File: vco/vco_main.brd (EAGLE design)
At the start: 94.9 x 107.9 mm, 101 parts, among them IC1 OPA4130U, IC2 LM13700M, IC3 OPA4130U, IC4 OPA4130U, Q1 MMBFJ3

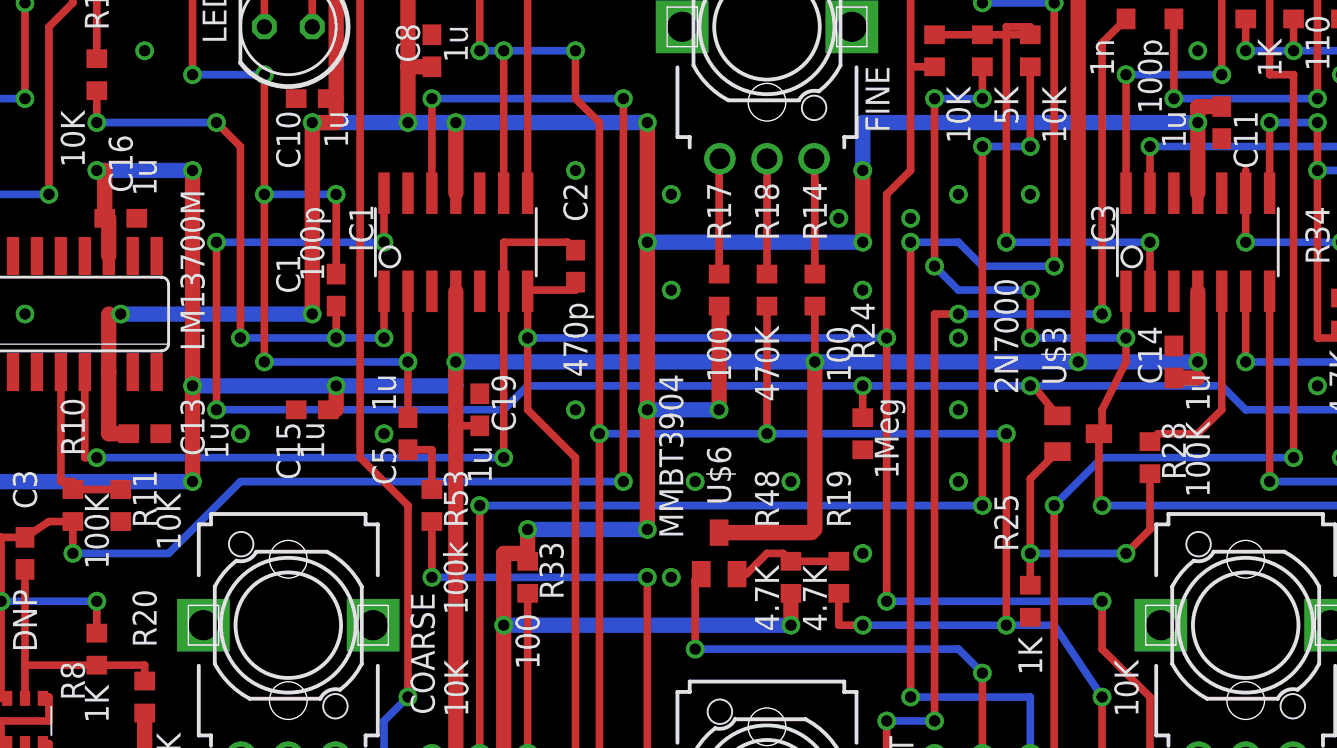
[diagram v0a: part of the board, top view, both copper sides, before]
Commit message: made some small changes that drove me crazy during assembly.
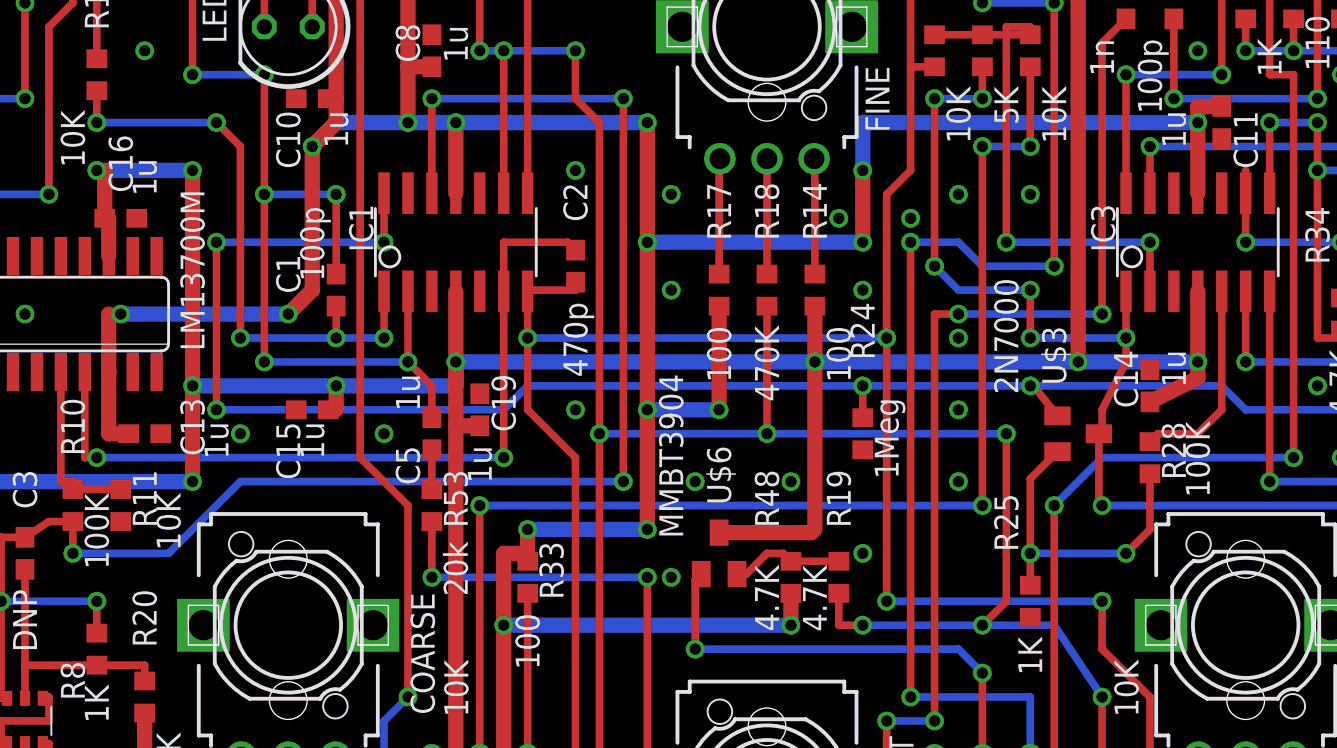
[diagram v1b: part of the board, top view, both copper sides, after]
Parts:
- R53: value 100k -> 20k
- moved C14 1.80 mm to (68.6, 67.3)
- moved C5 1.27 mm to (30.5, 64.8)
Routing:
- net +12V: track 255.3 -> 256.9 mm
- net N$48: track 3.38 -> 2.11 mm
- net -12V: track 342.7 -> 341.7 mm
- net N$5: track 195.6 -> 196.2 mm
- net N$3: track 67.6 -> 68.1 mm
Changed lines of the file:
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@@
 <setting verticaltext="up"/>
 </settings>
-<grid distance="0.5" unitdist="mil" unit="mil" style="lines" multiple="1" display="yes" altdistance="0.025" altunitdist="inch" altunit="inch"/>
+<grid distance="0.05" unitdist="inch" unit="inch" style="lines" multiple="1" display="no" altdistance="0.025" altunitdist="inch" altunit="inch"/>
 <layers>
 <layer number="1" name="Top" color="4" fill="1" visible="yes" active="yes"/>
@@
 </element>
 <element name="EXPMOD" library="dan" package="PJ301BM" value="PJ301BM" x="13.97" y="24.13" smashed="yes"/>
-<element name="C5" library="dan" package="C0603" value="1u" x="29.21" y="64.77" smashed="yes" rot="R270">
-<attribute name="NAME" x="27.305" y="64.135" size="1.27" layer="21" font="vector" ratio="15" rot="R270"/>
-<attribute name="VALUE" x="27.305" y="67.945" size="1.27" layer="21" font="vector" ratio="15" rot="R270"/>
+<element name="C5" library="dan" package="C0603" value="1u" x="30.48" y="64.77" smashed="yes" rot="R270">
+<attribute name="NAME" x="28.575" y="64.135" size="1.27" layer="21" font="vector" ratio="15" rot="R270"/>
+<attribute name="VALUE" x="28.575" y="67.945" size="1.27" layer="21" font="vector" ratio="15" rot="R270"/>
 </element>
 <element name="LINMOD" library="dan" package="PJ301BM" value="PJ301BM" x="31.75" y="8.89" smashed="yes"/>
@@
 <attribute name="VALUE" x="18.415" y="65.405" size="1.27" layer="21" font="vector" ratio="15" rot="R270"/>
 </element>
-<element name="C14" library="dan" package="C0603" value="1u" x="69.85" y="68.58" smashed="yes" rot="R90">
-<attribute name="NAME" x="67.945" y="70.485" size="1.27" layer="21" font="vector" ratio="15" rot="R270"/>
-<attribute name="VALUE" x="70.485" y="67.945" size="1.27" layer="21" font="vector" ratio="15" rot="R270"/>
+<element name="C14" library="dan" package="C0603" value="1u" x="68.58" y="67.31" smashed="yes" rot="R90">
+<attribute name="NAME" x="66.675" y="69.215" size="1.27" layer="21" font="vector" ratio="15" rot="R270"/>
+<attribute name="VALUE" x="69.215" y="69.215" size="1.27" layer="21" font="vector" ratio="15" rot="R270"/>
 </element>
 <element name="C15" library="dan" package="C0603" value="1u" x="24.13" y="66.04" smashed="yes" rot="R180">
@@
 <attribute name="VALUE" x="3.175" y="19.685" size="1.27" layer="21" font="vector" ratio="15" rot="R270"/>
 </element>
-<element name="R53" library="dan" package="R0603" value="100k" x="30.48" y="60.96" smashed="yes" rot="R90">
+<element name="R53" library="dan" package="R0603" value="20k" x="30.48" y="60.96" smashed="yes" rot="R90">
 <attribute name="NAME" x="31.115" y="62.865" size="1.27" layer="21" font="vector" ratio="15" rot="R270"/>
 <attribute name="VALUE" x="31.115" y="59.055" size="1.27" layer="21" font="vector" ratio="15" rot="R270"/>
@@
 <via x="25.4" y="77.47" extent="1-16" drill="0.6"/>
 <wire x1="25.4" y1="77.47" x2="25.4" y2="73.24" width="0.4064" layer="1"/>
-<wire x1="29.21" y1="68.58" x2="29.21" y2="65.62" width="0.4064" layer="1"/>
 <wire x1="7.62" y1="93.56" x2="7.62" y2="95.25" width="0.4064" layer="1"/>
 <via x="7.62" y="95.25" extent="1-16" drill="0.6"/>
@@
 <wire x1="7.62" y1="96.45" x2="7.62" y2="96.52" width="0.4064" layer="1"/>
 <wire x1="7.62" y1="96.45" x2="7.62" y2="95.25" width="0.4064" layer="1"/>
+<wire x1="30.48" y1="65.62" x2="30.48" y2="67.31" width="0.4064" layer="1"/>
+<wire x1="30.48" y1="67.31" x2="29.21" y2="68.58" width="0.4064" layer="1"/>
 </signal>
 <signal name="-12V">
@@
 <wire x1="71.12" y1="100.3935" x2="71.12" y2="97.79" width="0.8128" layer="1"/>
 <wire x1="71.12" y1="97.79" x2="76.62" y2="97.79" width="0.8128" layer="1"/>
-<via x="24.13" y="81.28" extent="1-16" drill="0.6"/>
-<wire x1="24.13" y1="81.28" x2="29.21" y2="81.28" width="0.8128" layer="16"/>
+<via x="24.13" y="80.01" extent="1-16" drill="0.6"/>
 <wire x1="72.39" y1="82.13" x2="71.12" y2="82.13" width="0.8128" layer="1"/>
 <wire x1="71.12" y1="82.13" x2="71.12" y2="81.28" width="0.8128" layer="1"/>
@@
 <contactref element="C13" pad="1"/>
 <contactref element="IC2" pad="6"/>
-<wire x1="24.13" y1="81.28" x2="24.13" y2="71.12" width="0.8128" layer="1"/>
-<via x="24.13" y="71.12" extent="1-16" drill="0.6"/>
-<wire x1="24.13" y1="71.12" x2="13.97" y2="71.12" width="0.8128" layer="16"/>
+<via x="22.86" y="71.12" extent="1-16" drill="0.6"/>
+<wire x1="22.86" y1="71.12" x2="13.97" y2="71.12" width="0.8128" layer="16"/>
 <via x="13.97" y="71.12" extent="1-16" drill="0.6"/>
 <wire x1="13.97" y1="71.12" x2="13.335" y2="71.12" width="0.4064" layer="1"/>
@@
 <wire x1="7.62" y1="90.17" x2="7.62" y2="91.86" width="0.8128" layer="1"/>
 <wire x1="25.4" y1="82.55" x2="25.4" y2="81.28" width="0.8128" layer="1"/>
-<wire x1="25.4" y1="81.28" x2="24.13" y2="81.28" width="0.8128" layer="1"/>
+<wire x1="25.4" y1="81.28" x2="24.13" y2="80.01" width="0.8128" layer="1"/>
 <wire x1="29.21" y1="101.6" x2="57.15" y2="101.6" width="0.8128" layer="16"/>
 <wire x1="53.34" y1="78.74" x2="53.34" y2="81.28" width="0.8128" layer="16"/>
@@
 <wire x1="49.53" y1="54.61" x2="34.29" y2="54.61" width="0.8128" layer="16"/>
 <via x="34.29" y="54.61" extent="1-16" drill="0.6"/>
+<wire x1="29.21" y1="81.28" x2="25.4" y2="81.28" width="0.8128" layer="16"/>
+<wire x1="25.4" y1="81.28" x2="24.13" y2="80.01" width="0.8128" layer="16"/>
+<wire x1="24.13" y1="80.01" x2="24.13" y2="72.39" width="0.8128" layer="1"/>
+<wire x1="24.13" y1="72.39" x2="22.86" y2="71.12" width="0.8128" layer="1"/>
 </signal>
 <signal name="+12V">
@@
 <wire x1="31.75" y1="68.58" x2="50.8" y2="68.58" width="0.8128" layer="16"/>
 <via x="50.8" y="68.58" extent="1-16" drill="0.6"/>
-<wire x1="50.8" y1="68.58" x2="50.8" y2="71.54" width="0.4064" layer="1"/>
+<wire x1="50.8" y1="68.58" x2="50.8" y2="71.54" width="0.8128" layer="1"/>
 <wire x1="71.12" y1="72.3265" x2="71.12" y2="68.58" width="0.8128" layer="1"/>
 <via x="71.12" y="68.58" extent="1-16" drill="0.6"/>
@@
 <contactref element="POWER" pad="10"/>
 <contactref element="POWER" pad="9"/>
-<wire x1="71.12" y1="67.73" x2="71.12" y2="68.58" width="0.4064" layer="1"/>
+<wire x1="71.12" y1="67.73" x2="71.12" y2="68.58" width="0.8128" layer="1"/>
 <via x="54.61" y="90.17" extent="1-16" drill="0.6"/>
 <via x="54.61" y="93.98" extent="1-16" drill="0.6"/>
@@
 <wire x1="46.99" y1="101.6" x2="46.57" y2="101.6" width="0.8128" layer="1"/>
 <contactref element="C19" pad="1"/>
-<wire x1="33.02" y1="65.19" x2="31.75" y2="65.19" width="0.4064" layer="1"/>
-<wire x1="69.85" y1="67.73" x2="71.12" y2="67.73" width="0.8128" layer="1"/>
+<wire x1="33.02" y1="65.19" x2="31.75" y2="65.19" width="0.8128" layer="1"/>
+<wire x1="68.58" y1="66.46" x2="71.12" y2="67.73" width="0.8128" layer="1"/>
 <wire x1="64.77" y1="95.67" x2="64.77" y2="91.44" width="0.8128" layer="1"/>
 <contactref element="IC2" pad="11"/>
@@
 <wire x1="48.26" y1="64.77" x2="60.96" y2="64.77" width="0.4064" layer="16"/>
 <via x="60.96" y="64.77" extent="1-16" drill="0.6"/>
-<wire x1="60.96" y1="64.77" x2="60.96" y2="54.61" width="0.4064" layer="1"/>
-<via x="60.96" y="54.61" extent="1-16" drill="0.6"/>
+<via x="59.69" y="54.61" extent="1-16" drill="0.6"/>
 <via x="66.04" y="50.8" extent="1-16" drill="0.6"/>
 <wire x1="66.04" y1="50.8" x2="66.04" y2="38.1" width="0.4064" layer="1"/>
@@
 <wire x1="52.07" y1="54.61" x2="53.34" y2="54.61" width="0.4064" layer="1"/>
 <via x="53.34" y="54.61" extent="1-16" drill="0.6"/>
-<wire x1="53.34" y1="54.61" x2="60.96" y2="54.61" width="0.4064" layer="16"/>
+<wire x1="53.34" y1="54.61" x2="59.69" y2="54.61" width="0.4064" layer="16"/>
 <wire x1="66.04" y1="50.8" x2="63.5" y2="54.61" width="0.4064" layer="16"/>
-<wire x1="63.5" y1="54.61" x2="60.96" y2="54.61" width="0.4064" layer="16"/>
+<wire x1="63.5" y1="54.61" x2="59.69" y2="54.61" width="0.4064" layer="16"/>
 <wire x1="66.04" y1="38.1" x2="67.31" y2="36.83" width="0.4064" layer="16"/>
 <wire x1="67.31" y1="36.83" x2="73.66" y2="36.83" width="0.4064" layer="16"/>
+<wire x1="60.96" y1="64.77" x2="60.96" y2="55.88" width="0.4064" layer="1"/>
+<wire x1="60.96" y1="55.88" x2="59.69" y2="54.61" width="0.4064" layer="1"/>
 </signal>
 <signal name="N$15">
@@
 <contactref element="C5" pad="2"/>
 <contactref element="R53" pad="2"/>
-<wire x1="29.21" y1="63.92" x2="30.48" y2="63.92" width="0.4064" layer="1"/>
 <wire x1="30.48" y1="63.92" x2="30.48" y2="61.81" width="0.4064" layer="1"/>
 </signal>

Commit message: changed a bunch of stuff.
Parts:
- moved R13 1.27 mm to (14.0, 95.2)
- renumbered SYNCSW to S1
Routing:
- net N$19: track 42.2 -> 43.9 mm, vias 2 -> 3
- net TRI: track 216.1 -> 217.4 mm, vias 12 -> 13
- net N$51: track 84.8 -> 83.5 mm
- net N$5: track 196.2 -> 197.4 mm
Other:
- board text added: "3300ppm"
- board text added: "C0G"
- board text removed: "tempco"
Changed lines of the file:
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@@
 <text x="40.64" y="12.7" size="1.778" layer="21" font="vector" ratio="15" rot="R270">linmod</text>
 <text x="40.64" y="27.94" size="1.778" layer="21" font="vector" ratio="15" rot="R270">sync</text>
-<text x="17.78" y="100.33" size="1.778" layer="21" font="vector" ratio="15" rot="R270">tempco</text>
+<text x="15.24" y="96.52" size="1.27" layer="21" font="vector" ratio="15" rot="R270">3300ppm</text>
 <wire x1="0" y1="107.9373" x2="0" y2="0" width="0" layer="20"/>
 <rectangle x1="48.19015" y1="18.33245" x2="48.30445" y2="18.34515" layer="22"/>
@@
 <rectangle x1="48.22825" y1="9.60755" x2="48.74895" y2="9.62025" layer="22"/>
 <rectangle x1="48.24095" y1="9.62025" x2="48.73625" y2="9.63295" layer="22"/>
+<text x="39.37" y="76.2" size="1.27" layer="21" font="vector" ratio="15" rot="R270">C0G</text>
 </plain>
 <attributes>
@@
 <attribute name="VALUE" x="23.495" y="38.735" size="1.27" layer="21" font="vector" ratio="15" rot="R270"/>
 </element>
-<element name="R13" library="dan" package="R0603" value="1.2k" x="15.24" y="95.25" smashed="yes" rot="R90">
-<attribute name="NAME" x="15.875" y="100.965" size="1.27" layer="21" font="vector" ratio="15" rot="R270"/>
-<attribute name="VALUE" x="14.605" y="93.345" size="1.27" layer="21" font="vector" ratio="15" rot="R270"/>
+<element name="R13" library="dan" package="R0603" value="1.2k" x="13.97" y="95.25" smashed="yes" rot="R90">
+<attribute name="NAME" x="14.605" y="100.965" size="1.27" layer="21" font="vector" ratio="15" rot="R270"/>
+<attribute name="VALUE" x="13.335" y="93.345" size="1.27" layer="21" font="vector" ratio="15" rot="R270"/>
 </element>
 <element name="COARSE" library="dan" package="EVUFXJ" value="10K" x="22.86" y="54.61" smashed="yes">
@@
 <element name="VPEROCT" library="dan" package="PJ301BM" value="PJ301BM" x="13.97" y="8.89" smashed="yes"/>
 <element name="C2" library="dan" package="C0603" value="470p" x="38.1" y="73.66" smashed="yes" rot="R270">
-<attribute name="NAME" x="37.465" y="78.105" size="1.27" layer="21" font="vector" ratio="15" rot="R270"/>
-<attribute name="VALUE" x="37.465" y="71.755" size="1.27" layer="21" font="vector" ratio="15" rot="R270"/>
+<attribute name="NAME" x="38.735" y="79.375" size="1.27" layer="21" font="vector" ratio="15" rot="R270"/>
+<attribute name="VALUE" x="38.735" y="71.755" size="1.27" layer="21" font="vector" ratio="15" rot="R270"/>
 </element>
 <element name="R20" library="dan" package="R0603" value="100K" x="15.24" y="50.8" smashed="yes" rot="R90">
@@
 <attribute name="VALUE" x="65.405" y="85.725" size="1.27" layer="21" font="vector" ratio="15" rot="R270"/>
 </element>
-<element name="SYNCSW" library="dan" package="255SB" value="" x="48.26" y="16.51" smashed="yes" rot="R90">
-<attribute name="NAME" x="51.816" y="20.828" size="1.27" layer="21" font="vector" ratio="15" rot="R270"/>
-<attribute name="VALUE" x="44.704" y="16.51" size="1.27" layer="27" ratio="10" rot="R90"/>
-</element>
 <element name="R47" library="dan" package="R0603" value="4.7K" x="24.13" y="95.25" smashed="yes" rot="R90">
 <attribute name="NAME" x="23.495" y="100.965" size="1.27" layer="21" font="vector" ratio="15" rot="R270"/>
@@
 <attribute name="VALUE" x="19.6596" y="88.1634" size="1.27" layer="27" ratio="10" rot="R180"/>
 </element>
+<element name="S1" library="dan" package="255SB" value="" x="48.26" y="16.51" rot="R90"/>
 </elements>
 <signals>
@@
 <via x="35.56" y="43.18" extent="1-16" drill="0.6"/>
 <via x="55.88" y="76.2" extent="1-16" drill="0.6"/>
-<via x="38.1" y="78.74" extent="1-16" drill="0.6"/>
+<via x="38.1" y="80.01" extent="1-16" drill="0.6"/>
 <via x="39.37" y="88.9" extent="1-16" drill="0.6"/>
 <via x="25.4" y="101.6" extent="1-16" drill="0.6"/>
@@
 <wire x1="63.5" y1="88.9" x2="63.5" y2="99.06" width="0.4064" layer="1"/>
 <wire x1="63.5" y1="99.06" x2="60.96" y2="101.6" width="0.4064" layer="1"/>
+<via x="38.1" y="71.12" extent="1-16" drill="0.8"/>
+<wire x1="38.1" y1="72.39" x2="38.1" y2="71.12" width="0.4064" layer="1"/>
 </signal>
 <signal name="N$11">
@@
 <contactref element="U$2" pad="2"/>
 <contactref element="R21" pad="2"/>
-<contactref element="SYNCSW" pad="2"/>
 <wire x1="8.89" y1="48.33" x2="8.89" y2="41.49" width="0.4064" layer="1"/>
 <via x="41.91" y="16.51" extent="1-16" drill="0.6"/>
-<wire x1="48.26" y1="16.51" x2="41.91" y2="16.51" width="0.4064" layer="16"/>
 <wire x1="10.16" y1="41.49" x2="10.16" y2="41.91" width="0.4064" layer="1"/>
 <wire x1="10.16" y1="41.49" x2="8.89" y2="41.49" width="0.4064" layer="1"/>
@@
 <via x="8.89" y="31.75" extent="1-16" drill="0.6"/>
 <wire x1="8.89" y1="31.75" x2="8.89" y2="41.49" width="0.4064" layer="1"/>
+<contactref element="S1" pad="2"/>
+<wire x1="48.26" y1="16.51" x2="41.91" y2="16.51" width="0.4064" layer="16"/>
 </signal>
 <signal name="N$14">
@@
 <contactref element="R13" pad="2"/>
 <contactref element="R18" pad="1"/>
-<via x="15.24" y="97.79" extent="1-16" drill="0.6"/>
-<wire x1="15.24" y1="97.79" x2="33.02" y2="97.79" width="0.4064" layer="16"/>
+<via x="13.97" y="97.79" extent="1-16" drill="0.6"/>
+<wire x1="13.97" y1="97.79" x2="33.02" y2="97.79" width="0.4064" layer="16"/>
 <via x="33.02" y="97.79" extent="1-16" drill="0.6"/>
 <wire x1="33.02" y1="97.79" x2="33.02" y2="85.09" width="0.4064" layer="1"/>
@@
 <via x="66.04" y="38.1" extent="1-16" drill="0.6"/>
 <via x="73.66" y="36.83" extent="1-16" drill="0.6"/>
-<wire x1="15.24" y1="96.1" x2="15.24" y2="97.79" width="0.4064" layer="1"/>
+<wire x1="13.97" y1="96.1" x2="13.97" y2="97.79" width="0.4064" layer="1"/>
 <contactref element="R19" pad="1"/>
 <contactref element="R46" pad="1"/>
@@
 <contactref element="IC1" pad="8"/>
 <contactref element="R4" pad="2"/>
-<wire x1="15.24" y1="94.4" x2="15.24" y2="88.9" width="0.4064" layer="1"/>
-<via x="15.24" y="88.9" extent="1-16" drill="0.6"/>
+<wire x1="13.97" y1="94.4" x2="13.97" y2="88.9" width="0.4064" layer="1"/>
+<via x="13.97" y="88.9" extent="1-16" drill="0.6"/>
 <via x="8.89" y="87.63" extent="1-16" drill="0.6"/>
 <wire x1="8.89" y1="87.63" x2="8.89" y2="82.55" width="0.4064" layer="1"/>
@@
 <via x="6.35" y="82.55" extent="1-16" drill="0.6"/>
 <wire x1="6.35" y1="82.55" x2="6.35" y2="84.24" width="0.4064" layer="1"/>
-<wire x1="15.24" y1="88.9" x2="35.56" y2="88.9" width="0.4064" layer="16"/>
+<wire x1="13.97" y1="88.9" x2="35.56" y2="88.9" width="0.4064" layer="16"/>
 <via x="35.56" y="88.9" extent="1-16" drill="0.6"/>
 <wire x1="35.56" y1="88.9" x2="35.56" y2="77.5335" width="0.4064" layer="1"/>
-<wire x1="15.24" y1="88.9" x2="10.16" y2="88.9" width="0.4064" layer="16"/>
+<wire x1="13.97" y1="88.9" x2="10.16" y2="88.9" width="0.4064" layer="16"/>
 <wire x1="10.16" y1="88.9" x2="8.89" y2="87.63" width="0.4064" layer="16"/>
 </signal>
@@
 <wire x1="34.29" y1="72.3265" x2="34.29" y2="74.93" width="0.4064" layer="1"/>
 <wire x1="34.29" y1="74.93" x2="37.68" y2="74.93" width="0.4064" layer="1"/>
+<wire x1="38.1" y1="74.93" x2="37.68" y2="74.93" width="0.4064" layer="1"/>
 <wire x1="37.68" y1="74.93" x2="38.1" y2="74.51" width="0.4064" layer="1"/>
+<via x="38.1" y="76.2" extent="1-16" drill="0.8"/>
+<wire x1="38.1" y1="76.2" x2="38.1" y2="74.93" width="0.4064" layer="1"/>
 </signal>
 <signal name="N$23">
@@
 <signal name="N$51">
 <contactref element="C7" pad="2"/>
-<contactref element="SYNCSW" pad="3"/>
 <wire x1="67.31" y1="86.78" x2="66.04" y2="85.51" width="0.4064" layer="1"/>
 <wire x1="66.04" y1="85.51" x2="66.04" y2="71.12" width="0.4064" layer="1"/>
@@
 <wire x1="57.15" y1="71.12" x2="58.42" y2="71.12" width="0.4064" layer="1"/>
 <wire x1="54.61" y1="33.02" x2="48.26" y2="33.02" width="0.4064" layer="16"/>
-<wire x1="48.26" y1="20.32" x2="48.26" y2="33.02" width="0.4064" layer="1"/>
 <wire x1="54.61" y1="49.53" x2="54.61" y2="33.02" width="0.4064" layer="1"/>
+<contactref element="S1" pad="3"/>
+<wire x1="48.26" y1="21.59" x2="48.26" y2="33.02" width="0.4064" layer="1"/>
 </signal>
 <signal name="N$52">
@@
 </signal>
 </signals>
+<errors>
+</errors>
 </board>
 </drawing>
